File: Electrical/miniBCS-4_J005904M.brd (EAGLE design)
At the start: 146.1 x 146.1 mm, 167 parts, among them IC1 WIZ850io, J14 A0/A1, J2 1734035-2, J3 RCA_DUAL, M2 TEENSY4.1, U1 ADA4084, U10 MAX11300GCM, U11 CAT811, U2 2G17, U3 ISL23425, U4 AD9833, U5 ISO1H815G, U6 78L12, U7 ADM3312/5, U8 2G17, U9 79L12, X1 OSC-OE-CFPS-9, X2 2520-

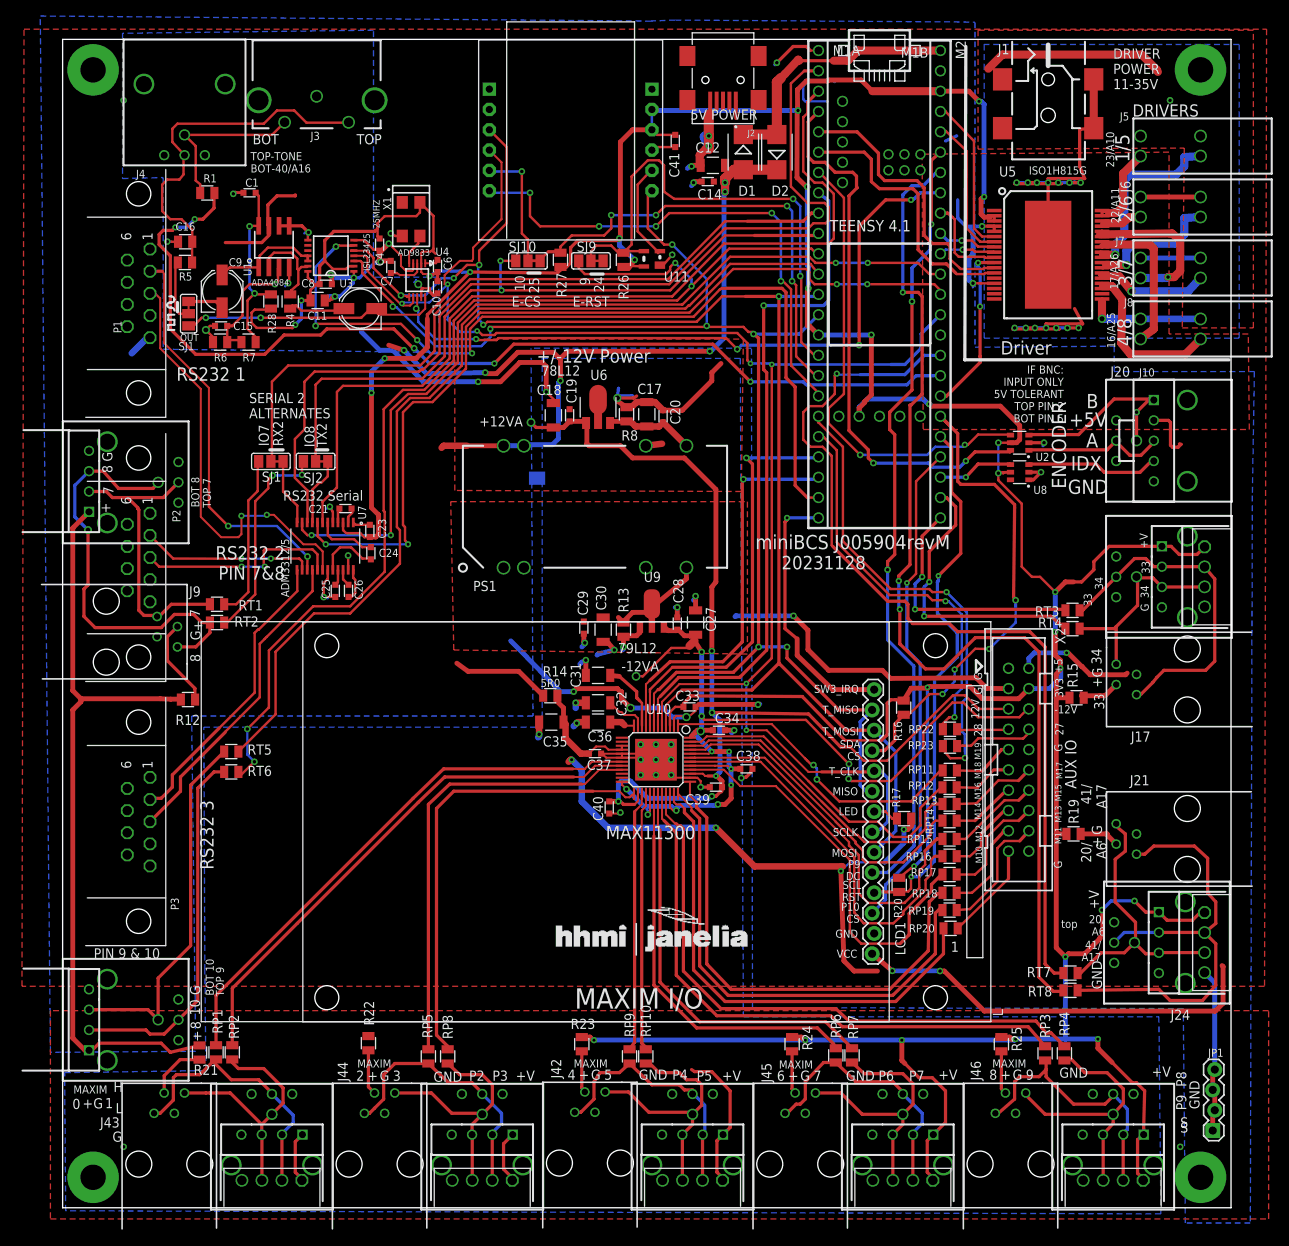
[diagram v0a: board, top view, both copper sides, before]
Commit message: Board Update 20240508
Add qwiic and SPI external connections
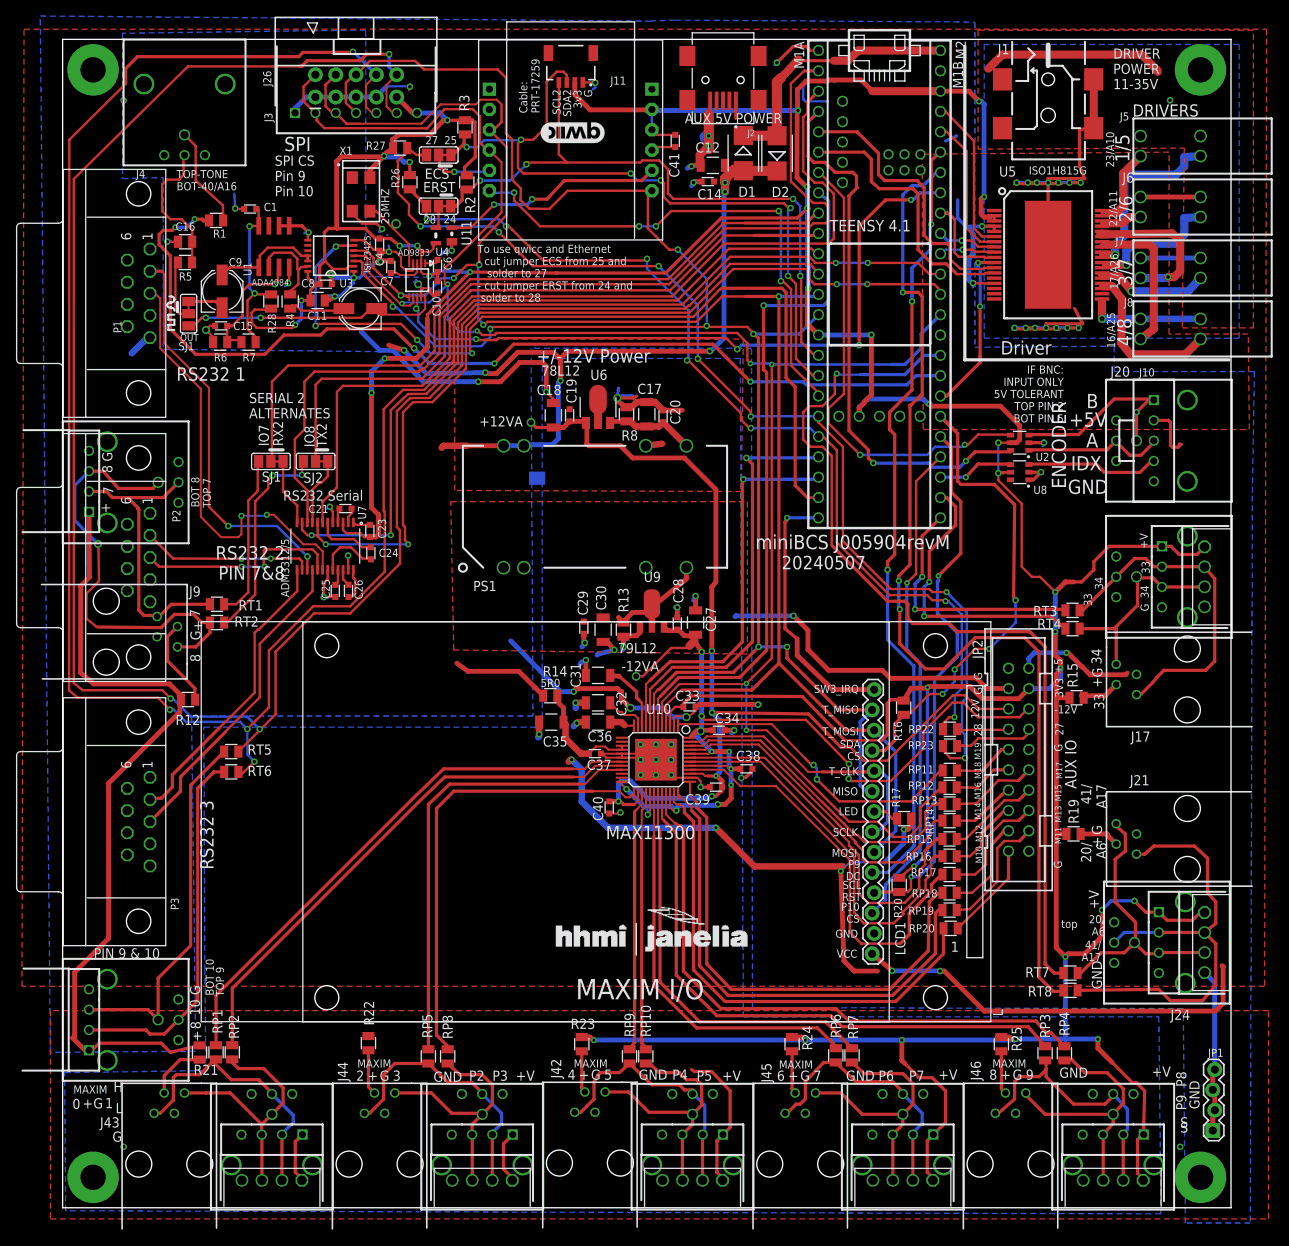
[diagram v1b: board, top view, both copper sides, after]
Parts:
- removed SJ10, SJ9: (no value), jumper:SJ_2
- added 25MHZ: (no value), STEVES_BU:PAD032
- added ECS, ERST: (no value), jumper:SJ_2
- added J11: QWIIC_RIGHT_ANGLE, SparkFun-Connectors:JST04_1MM_RA
- added J26: (no value), STEVES_BU:2X5SHROUDED-RATH
- added LOGO1: QWIIC_LOGO_8MM, SparkFun-Aesthetics:QWIIC_8MM
- added R2, R3: 4K99, SteveS:0805S
- J3: value RCA_DUAL -> (none); device STEVES_BU:RCJ-22XX -> STEVES_BU:AMPMODU7-RATH
- R26, R27: value 10K0 -> 4K99
- moved R26 28.4 mm to (43.4, 128.2), turned to 270 degrees
- moved U11 26.2 mm to (47.7, 121.5)
- moved R27 24.4 mm to (42.2, 132.5), turned to 0 degrees
- moved X1 6.97 mm to (37.3, 126.7)
- moved J3 5.35 mm to (36.7, 136.9)
- moved R1 3.60 mm to (19.2, 123.4), turned to 0 degrees
- moved C1 2.03 mm to (23.4, 124.8)
- moved D2 0.15 mm to (89.3, 131.8)
- moved D1 0.13 mm to (85.1, 131.8)
- renumbered X2 to JP2
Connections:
- net N$52 renamed ERST
- removed net ETH_CS: IC1.J1.5, M2.25, R27.2, SJ10.2, SJ10.3
- removed net ETH_RST: M2.24, R26.2, SJ9.2, SJ9.3, U11.3
- removed net MISO: IC1.J2.6, LCD1.13, LCD1.9, M2.12/MISO, U10.7, U3.3
- removed net MOSI: IC1.J1.3, LCD1.12, LCD1.6, M2.11/MOSI, U10.4, U3.5, U4.6
- removed net PIN_27: M2.27, RP23.1
- removed net PIN_28: M2.28, RP22.1
- new net CIPO: IC1.J2.6, J26.6, J3.4, LCD1.13, LCD1.9, M2.12/MISO, U10.7, U3.3
- new net COPI: IC1.J1.3, J26.4, J3.3, LCD1.12, LCD1.6, M2.11/MOSI, U10.4, U3.5, U4.6
- new net ETH_CS/SDA2: ECS.2, ECS.3, IC1.J1.5, J11.3, M2.25, R3.2
- new net ETH_RST/SCL2: ERST.2, ERST.3, J11.4, M2.24, R2.2, U11.3
- new net PIN27/ALT_ECS: ECS.1, M2.27, R27.2, RP23.1
- new net PIN28/ALT_ERST: ERST.1, M2.28, R26.2, RP22.1
- net +3V3D: now also J11.2, J26.9, J3.7, R2.1, R3.1
- net AGND: no longer J3.1
- net DAC0_OUT: no longer J3.2
- net DDS_OUT: no longer J3.3
- net DGND: now also J11.1, J26.1, J26.3, J26.5, J26.7, J3.1
- net N$13: now also 25MHZ.P$1
- net PIN10: now also J26.10, J3.6
- net PIN9: now also J26.8, J3.5; no longer SJ9.1
- net SCLK: now also J26.2, J3.2
- net TX2: no longer SJ10.1
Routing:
- net CIPO: track 0.00 -> 237.0 mm, vias 0 -> 7
- net COPI: track 0.00 -> 223.6 mm, vias 0 -> 5
- net MOSI: track 190.6 -> 0.00 mm, vias 5 -> 0
- net MISO: track 176.8 -> 0.00 mm, vias 7 -> 0
- net PIN10: track 117.7 -> 261.3 mm, vias 0 -> 3
- net PIN27/ALT_ECS: track 0.00 -> 136.7 mm, vias 0 -> 7
- net PIN9: track 140.9 -> 267.6 mm
- net PIN28/ALT_ERST: track 0.00 -> 120.1 mm, vias 0 -> 7
- net ETH_CS/SDA2: track 0.00 -> 99.6 mm, vias 0 -> 7
- net ETH_RST/SCL2: track 0.00 -> 86.1 mm, vias 0 -> 4
- net ETH_CS: track 76.9 -> 0.00 mm, vias 5 -> 0
- net ETH_RST: track 66.6 -> 0.00 mm, vias 2 -> 0
- net +3V3D: track 745.2 -> 803.7 mm, vias 30 -> 34
- net PIN_27: track 58.3 -> 0.00 mm, vias 2 -> 0
- net PIN_28: track 49.7 -> 0.00 mm, vias 2 -> 0
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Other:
- board text added: "20240507"
- board text added: "3v3"
- board text added: "AUX 5V POWER"
- board text added: "Cable: PRT-17259"
- board text added: "SCL2"
- board text added: "SDA2"
- board text added: "SPI"
- board text added: "SPI CS Pin 9 Pin 10"
- board text added: "To use qwicc and Ethernet - cut jumper ECS from 25 and solder to 27 - cut jumper ERST from 24 and solder to 28"
- board text removed: "20231128"
- board text removed: "25MHZ"
- board text removed: "5V POWER"
- board text removed: "E-CS"
- board text removed: "E-RST"
